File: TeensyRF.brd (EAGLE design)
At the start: 50 x 50 mm, 9 parts, among them X1 SMA-142-0701-801/806, X2 SMA-142-0701-801/806

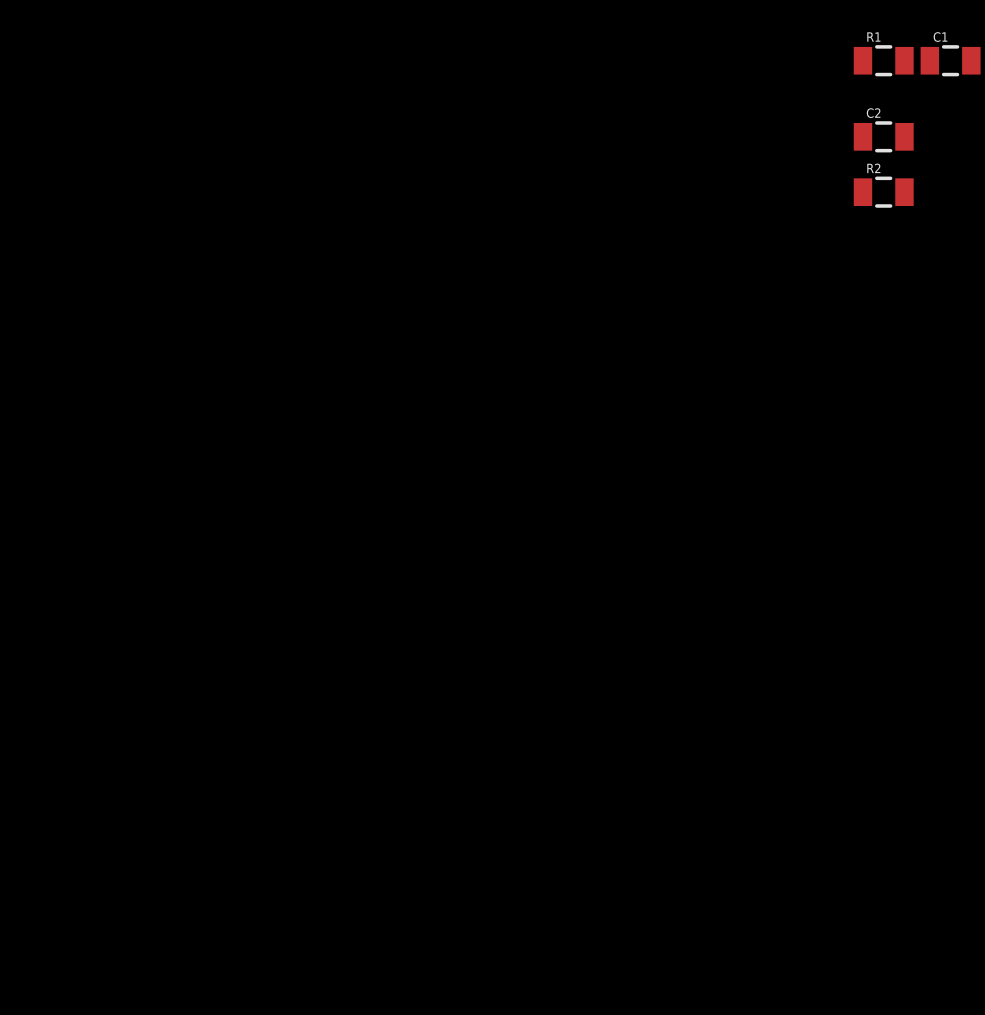
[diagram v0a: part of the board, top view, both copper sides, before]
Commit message: Finished TX schematic
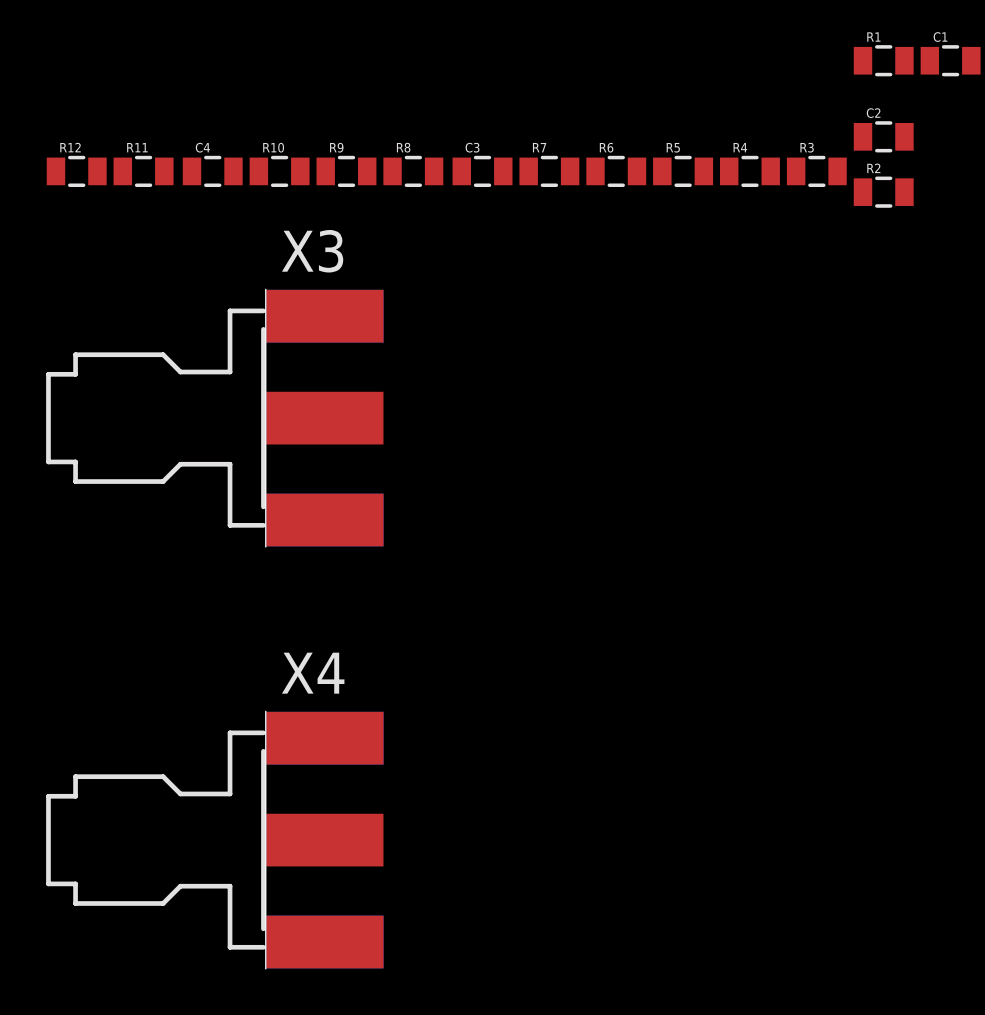
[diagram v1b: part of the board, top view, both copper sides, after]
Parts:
- added C3, C4: 0.1uF, SparkFun-Capacitors:0805
- added R10, R3, R4, R5, R6, R7, R8, R9: 100R, SparkFun-Resistors:0805
- added R11: 1.5k, SparkFun-Resistors:0805
- added R12: 2k, SparkFun-Resistors:0805
- added X3, X4: SMA-142-0701-801/806, con-coax:J502-ND-142-0701-801/806
- C1, C2: value (none) -> 1000pF
- R1, R2: value (none) -> 15k
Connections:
- new net BBI+: R7.1, U$2.P4, X1.1
- new net BBI-: R9.1, U$2.P5, X2.1
- new net BBQ+: R3.1, U$3.P4, X3.1
- new net BBQ-: R5.1, U$3.P5, X4.1
- new net N$11: R7.2, R8.2, U$2.P1
- new net N$13: R10.2, R9.2, U$2.P8
- new net N$6: R5.2, R6.2, U$3.P8
- new net N$8: R3.2, R4.2, U$3.P1
- new net NPD1: U$1.22/A8, U$2.P7
- new net NPD2: U$1.23/A9, U$3.P7
- new net VCM: C3.1, C4.1, R11.1, R12.2, U$2.P2, U$3.P2
- net 3.3V: now also R11.2, U$2.P3, U$3.P3
- net GND: now also C3.2, C4.2, R12.1, R4.1, R8.1, U$2.P6, U$2.PAD, U$3.P6, U$3.PAD, X1.G@1, X1.G@2, X1.G@3, X1.G@4, X2.G@1, X2.G@2, X2.G@3, X2.G@4, X3.G@1, X3.G@2, X3.G@3, X3.G@4, X4.G@1, X4.G@2, X4.G@3, X4.G@4
- net N$2: now also R10.1
- net N$4: now also R6.1

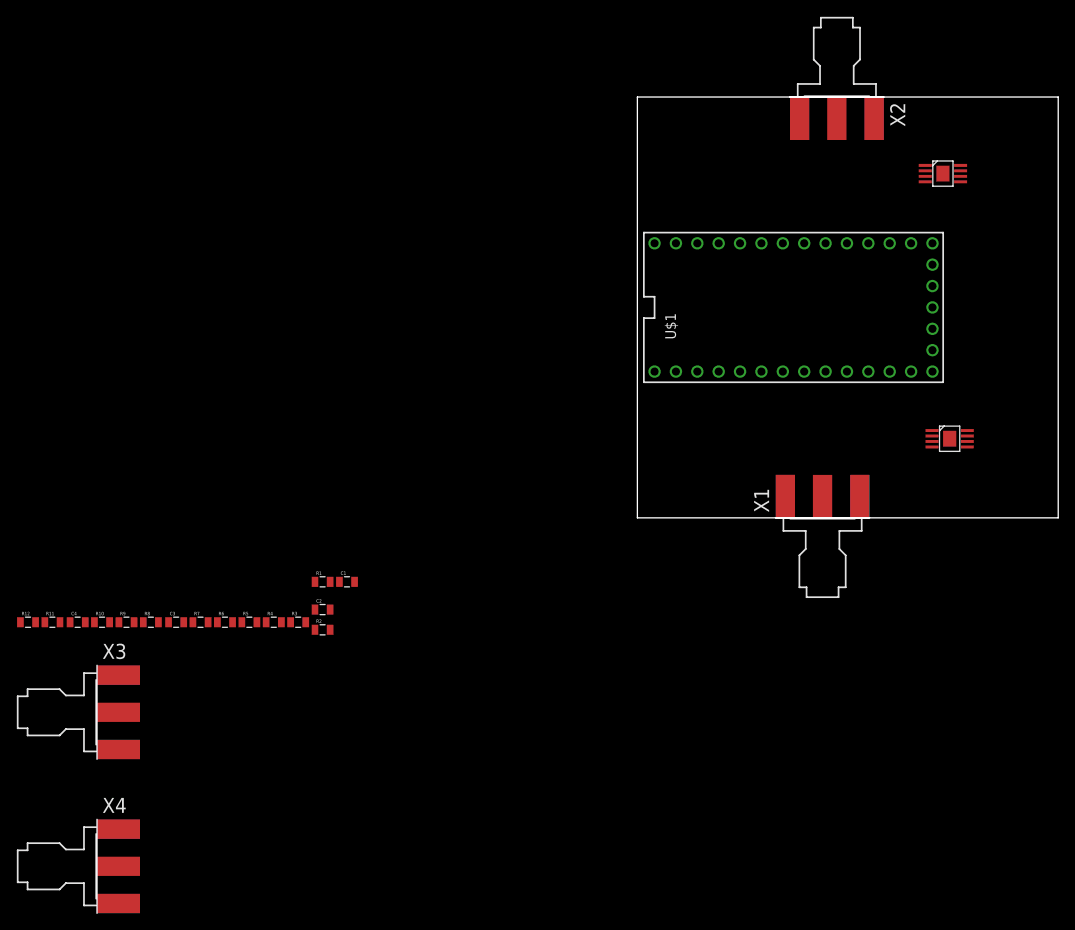
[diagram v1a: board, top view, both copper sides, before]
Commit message: Finished TX Test board layout
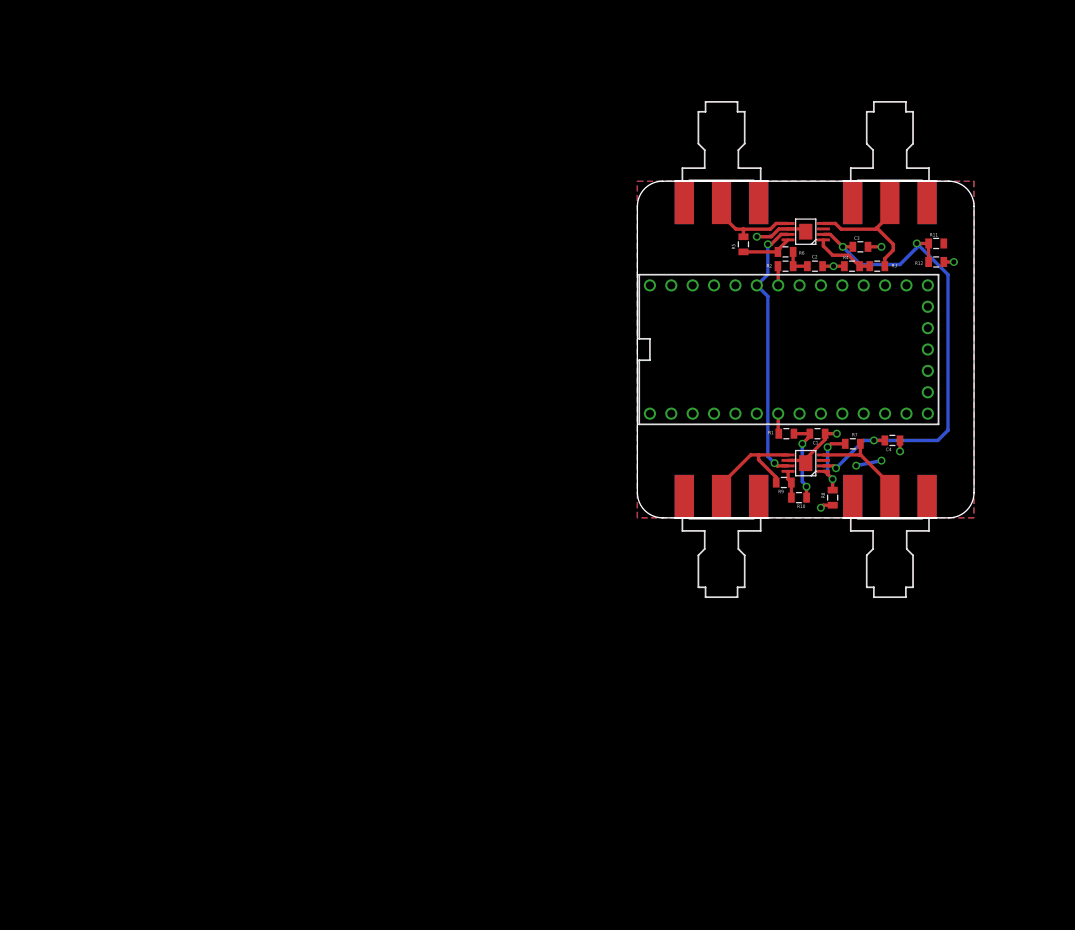
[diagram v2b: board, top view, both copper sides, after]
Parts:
- moved R12 116.1 mm to (35.5, 30.4), turned to 180 degrees
- moved R11 114.2 mm to (35.5, 32.6)
- moved X3 113.4 mm to (30.0, 40.0), turned to 270 degrees
- moved X4 110.1 mm to (10.0, 40.0), turned to 270 degrees
- moved C4 99.2 mm to (30.3, 9.20)
- moved C3 92.7 mm to (26.5, 32.2)
- moved R10 84.1 mm to (19.2, 2.40), turned to 180 degrees
- moved R8 82.3 mm to (23.2, 2.40), turned to 90 degrees
- moved R3 80.8 mm to (28.5, 29.9), turned to 180 degrees
- moved R4 80.7 mm to (25.5, 29.9)
- moved R7 80.3 mm to (25.6, 8.80), turned to 180 degrees
- moved R9 79.8 mm to (17.4, 4.20)
- moved R6 79.8 mm to (17.6, 31.6), turned to 180 degrees
- moved R5 73.9 mm to (12.6, 32.5), turned to 270 degrees
- moved C2 71.3 mm to (21.1, 29.9)
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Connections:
- removed net NPD1: U$1.22/A8, U$2.P7
- removed net NPD2: U$1.23/A9, U$3.P7
- new net NPD: U$1.21/A7, U$2.P7, U$3.P7
- net BBI+: now also R3.1, U$3.P4, X3.1; no longer R7.1, U$2.P4, X1.1
- net BBI-: now also R5.1, U$3.P5, X4.1; no longer R9.1, U$2.P5, X2.1
- net BBQ+: now also R7.1, U$2.P4, X1.1; no longer R3.1, U$3.P4, X3.1
- net BBQ-: now also R9.1, U$2.P5, X2.1; no longer R5.1, U$3.P5, X4.1
- net N$3: now also U$1.20/A6; no longer U$1.6
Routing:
- net VCM: track 0.00 -> 60.5 mm, vias 0 -> 4
- net NPD: track 0.00 -> 32.0 mm, vias 0 -> 2
- net GND: track 0.00 -> 24.6 mm, vias 0 -> 7
- net BBI+: track 0.00 -> 16.1 mm
- net BBQ-: track 0.00 -> 14.9 mm
- net BBQ+: track 0.00 -> 12.1 mm
- net BBI-: track 0.00 -> 11.2 mm
- net N$2: track 0.00 -> 10.0 mm, vias 0 -> 2
- net N$11: track 0.00 -> 9.10 mm, vias 0 -> 2
- net N$8: track 0.00 -> 7.22 mm
- net N$6: track 0.00 -> 6.02 mm
- net N$4: track 0.00 -> 3.40 mm
- net N$13: track 0.00 -> 3.29 mm
- net 3.3V: track 0.00 -> 3.06 mm, vias 0 -> 2
- net N$1: track 0.00 -> 2.43 mm
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- added copper zone on layer 1, net 3.3V
- added copper zone on layer 16, net GND
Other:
- board size 50 x 50 mm -> 40 x 40 mm
